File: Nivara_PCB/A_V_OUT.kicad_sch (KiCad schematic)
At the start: 9 parts, among them Q1 IRLML0040, U8 LTV-357T

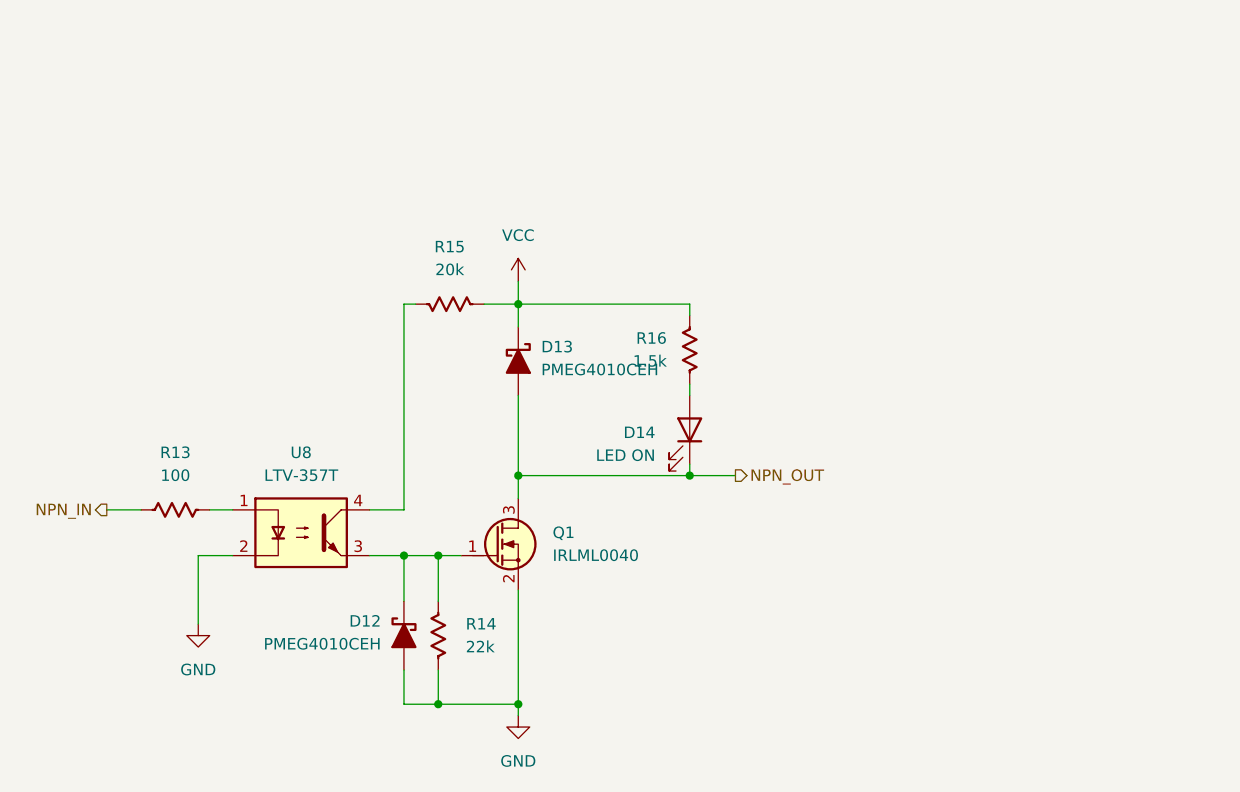
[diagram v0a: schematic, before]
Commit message: Cambios realizados en el PCB y el esquema de Nivara_PCB.
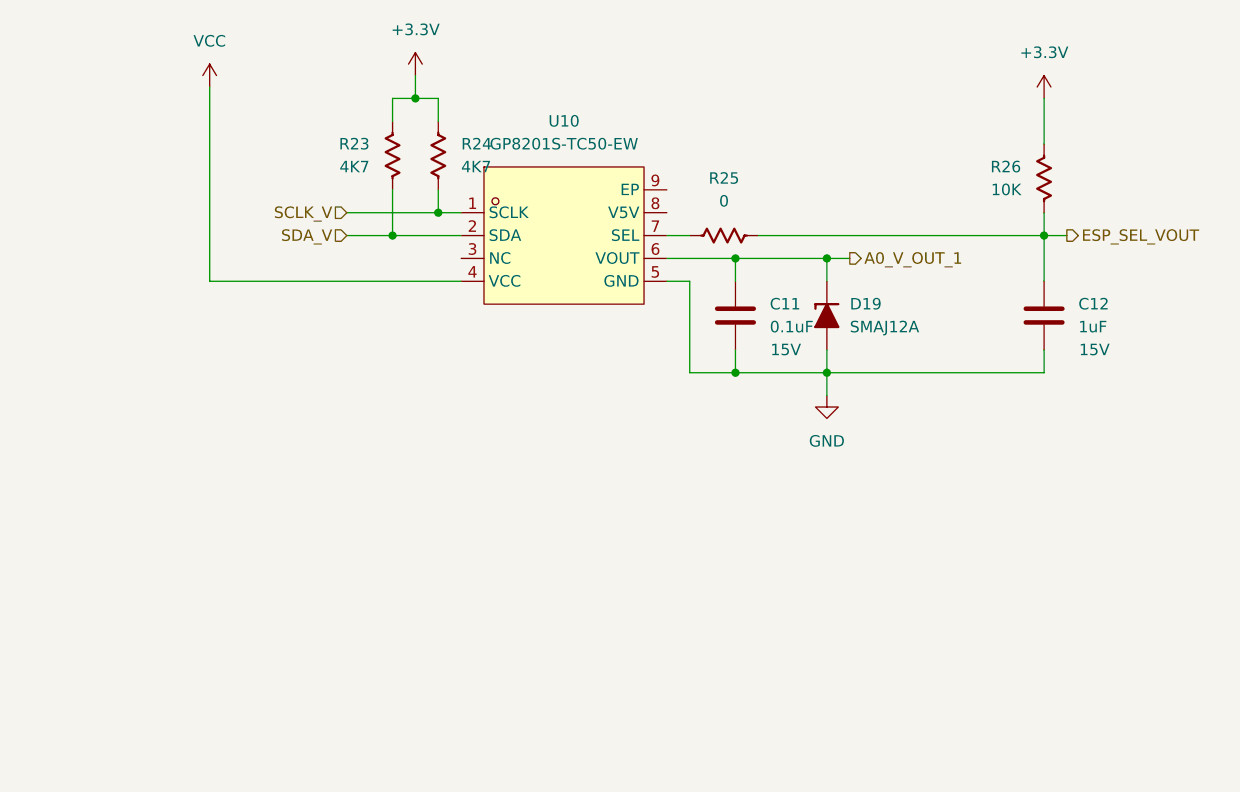
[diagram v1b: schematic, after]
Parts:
- removed D12, D13: PMEG4010CEH, PCM_Diode_SMD_AKL:D_SOD-123F, symbol PCM_Diode_Schottky_AKL:PMEG4010CEH
- removed D14: LED ON, LED_SMD:LED_0603_1608Metric, symbol Device:LED
- removed Q1: IRLML0040, PCM_Package_TO_SOT_SMD_AKL:SOT-23, symbol PCM_Transistor_MOSFET_AKL:IRLML0040
- removed R13: 100, PCM_Resistor_SMD_AKL:R_0603_1608Metric, symbol PCM_Resistor_US_AKL:R_0603
- removed R14: 22k, PCM_Resistor_SMD_AKL:R_0603_1608Metric, symbol PCM_Resistor_US_AKL:R_0603
- removed R15: 20k, PCM_Resistor_SMD_AKL:R_0603_1608Metric, symbol PCM_Resistor_US_AKL:R_0603
- removed R16: 1.5k, PCM_Resistor_SMD_AKL:R_0603_1608Metric, symbol PCM_Resistor_US_AKL:R_0603
- removed U8: LTV-357T, Package_SO:SO-4_4.4x3.6mm_P2.54mm, symbol Isolator:LTV-357T
- added C11: 0.1uF, PCM_Capacitor_SMD_AKL:C_0603_1608Metric, symbol PCM_Capacitor_US_AKL:C_0603
- added C12: 1uF, PCM_Capacitor_SMD_AKL:C_0603_1608Metric, symbol PCM_Capacitor_US_AKL:C_0603
- added D19: SMAJ12A, PCM_Diode_SMD_AKL:D_SMA, symbol PCM_Diode_TVS_AKL:SMAJ12A
- added R23, R24: 4K7, PCM_Resistor_SMD_AKL:R_0603_1608Metric, symbol PCM_Resistor_US_AKL:R_0603
- added R25: 0, PCM_Resistor_SMD_AKL:R_0603_1608Metric, symbol PCM_Resistor_US_AKL:R_0603
- added R26: 10K, PCM_Resistor_SMD_AKL:R_0603_1608Metric, symbol PCM_Resistor_US_AKL:R_0603
- added U10: GP8201S-TC50-EW, EasyEDA:ESOP-8_L4.9-W3.9-P1.27-LS6.0-BL-EP, symbol EasyEDA:GP8201S-TC50-EW
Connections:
- net GND: now also C11.2, C12.2, D19.2 (A), U10.5 (GND)
- net VCC: now also U10.4 (VCC)
- new net: R25.1, U10.7 (SEL)
- new net +3.3V: R23.1, R24.1, R26.1
- new net A0_V_OUT_1: C11.1, D19.1 (K), U10.6 (VOUT)
- new net ESP_SEL_VOUT: C12.1, R25.2, R26.2
- new net SCLK_V: R24.2, U10.1 (SCLK)
- new net SDA_V: R23.2, U10.2 (SDA)

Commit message: Cambios realizados en los archivos de Nivara_PCB.
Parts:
- C11, C12: symbol PCM_Capacitor_US_AKL:C_0603 -> EasyEDA:C_0603
- D19: symbol PCM_Diode_TVS_AKL:SMAJ12A -> EasyEDA:SMAJ12A
- R23, R24, R25, R26: symbol PCM_Resistor_US_AKL:R_0603 -> EasyEDA:R_0603
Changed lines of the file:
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@@
 	)
 	(symbol
-		(lib_id "PCM_Resistor_US_AKL:R_0603")
+		(lib_id "EasyEDA:R_0603")
 		(at 80.01 58.42 0)
 		(mirror y)
@@
 	)
 	(symbol
-		(lib_id "power:GND")
+		(lib_id "EasyEDA:GND")
 		(at 128.27 85.09 0)
 		(unit 1)
@@
 	)
 	(symbol
-		(lib_id "power:+3.3V")
+		(lib_id "EasyEDA:+3.3V")
 		(at 82.55 49.53 0)
 		(unit 1)
@@
 	)
 	(symbol
-		(lib_id "power:VCC")
+		(lib_id "EasyEDA:VCC")
 		(at 59.69 50.8 0)
 		(unit 1)
@@
 	)
 	(symbol
-		(lib_id "PCM_Resistor_US_AKL:R_0603")
+		(lib_id "EasyEDA:R_0603")
 		(at 152.4 60.96 0)
 		(mirror y)
@@
 	)
 	(symbol
-		(lib_id "PCM_Capacitor_US_AKL:C_0603")
+		(lib_id "EasyEDA:C_0603")
 		(at 152.4 76.2 0)
 		(unit 1)
@@
 	)
 	(symbol
-		(lib_id "PCM_Diode_TVS_AKL:SMAJ12A")
+		(lib_id "EasyEDA:SMAJ12A")
 		(at 128.27 76.2 90)
 		(unit 1)
@@
 	)
 	(symbol
-		(lib_id "PCM_Capacitor_US_AKL:C_0603")
+		(lib_id "EasyEDA:C_0603")
 		(at 118.11 76.2 0)
 		(unit 1)
@@
 	)
 	(symbol
-		(lib_id "PCM_Resistor_US_AKL:R_0603")
+		(lib_id "EasyEDA:R_0603")
 		(at 85.09 58.42 0)
 		(unit 1)
@@
 	)
 	(symbol
-		(lib_id "power:+3.3V")
+		(lib_id "EasyEDA:+3.3V")
 		(at 152.4 52.07 0)
 		(unit 1)
@@
 	)
 	(symbol
-		(lib_id "PCM_Resistor_US_AKL:R_0603")
+		(lib_id "EasyEDA:R_0603")
 		(at 116.84 67.31 90)
 		(unit 1)
